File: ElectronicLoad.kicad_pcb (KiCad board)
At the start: 4 copper layers, 100 x 65 mm, 96 parts, among them J1 USB_B, J2 Load, J3 AUX1, J4 TagConnect, J5 ICSP, Q1 MTP3055VL, Q2 DMG2302U, SW2 RESET, SW3 BOOTLOADER, SW4 Control, U1 TLC272, U2 NUP2114, U3 ATmega32U4-AU, U4 MCP1501-20, U5 MCP4726A3T, U6 INA220, U7 PCT2075D, U8 PCT2075D, Y1 16MHz

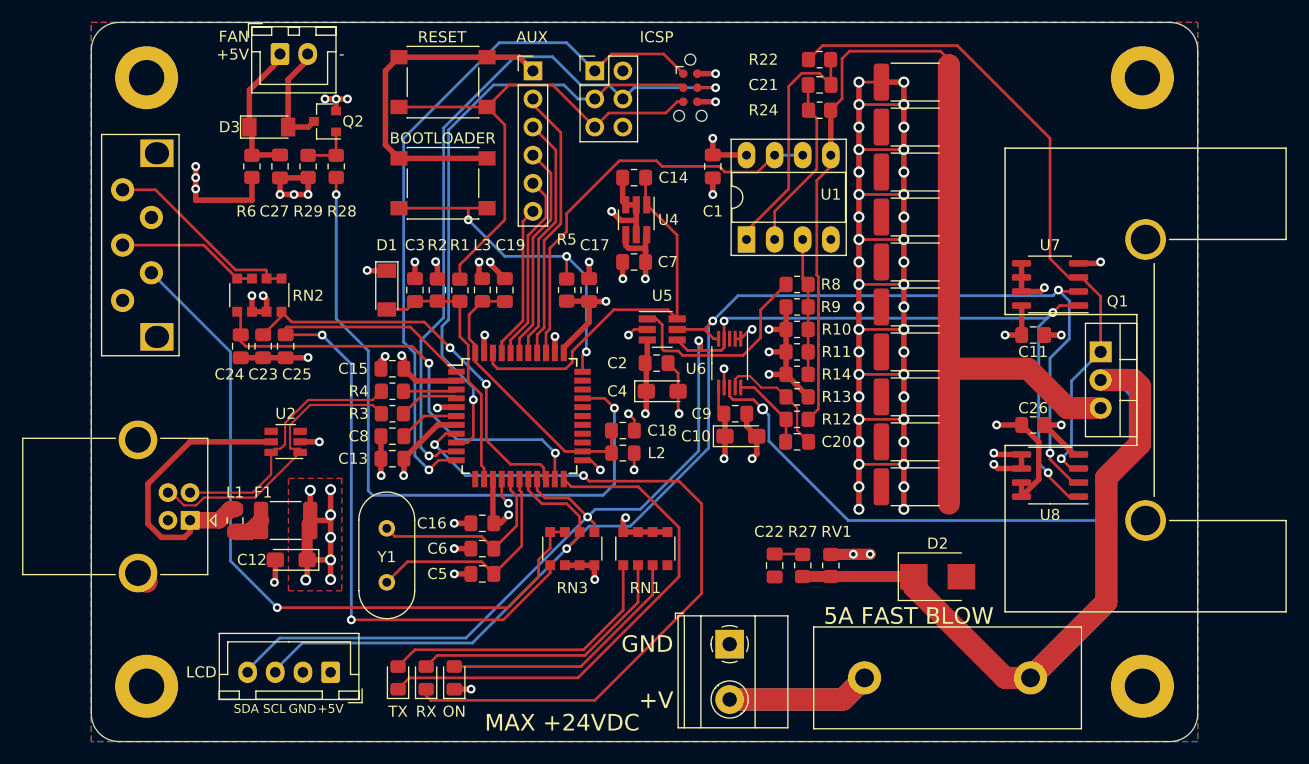
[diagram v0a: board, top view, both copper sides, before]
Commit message: Reduced decoupling capacitance on VBUS to <10uF
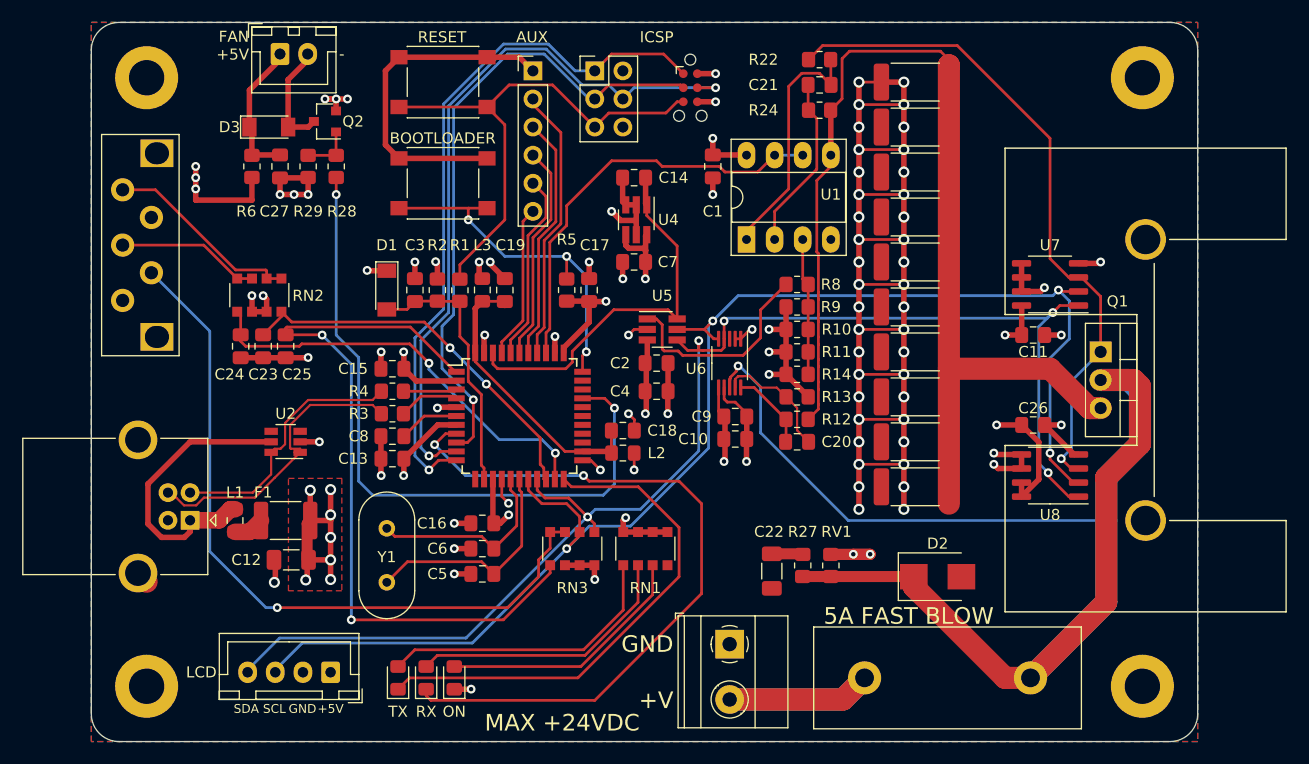
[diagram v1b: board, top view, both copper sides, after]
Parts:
- C10, C4: value 10μF -> 1μF; footprint Capacitor_Tantalum_SMD:CP_EIA-3216-18_Kemet-A_Pad1.58x1.35mm_HandSolder -> Capacitor_SMD:C_0805_2012Metric_Pad1.18x1.45mm_HandSolder
- C12: value 10μF -> 2.2μF; footprint Capacitor_Tantalum_SMD:CP_EIA-3216-18_Kemet-A_Pad1.58x1.35mm_HandSolder -> Capacitor_SMD:C_1206_3216Metric_Pad1.33x1.80mm_HandSolder
- C22: footprint Capacitor_SMD:C_0805_2012Metric_Pad1.18x1.45mm_HandSolder -> Capacitor_SMD:C_1206_3216Metric_Pad1.33x1.80mm_HandSolder
- moved C22 0.57 mm to (111.5, 164.6)
- moved C10 0.57 mm to (108.2, 152.7)
- moved C4 0.51 mm to (101.1, 148.3)
- moved C9 0.25 mm to (108.2, 150.6)
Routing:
- net /SCK: track 54.9 -> 58.2 mm
- net VLOAD: track 134.4 -> 137.3 mm
- net ROT_B: track 40.4 -> 38.3 mm
- net ROT_A: track 36.5 -> 34.9 mm
- net /MOSI: track 64.3 -> 65.8 mm
- net GND: track 301.8 -> 303.1 mm, vias 84 -> 83
- net /MISO: track 65.0 -> 63.8 mm
- net Net-(RN3-Pad3): track 65.6 -> 66.2 mm
- net VCC: track 122.0 -> 122.5 mm

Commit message: Cleanup
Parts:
- removed the C19 at (87.4, 139.2)
- removed J3: AUX1, Connector_PinHeader_2.54mm:PinHeader_1x06_P2.54mm_Vertical
- removed L2: 10μH, Inductor_SMD:L_0805_2012Metric_Pad1.15x1.40mm_HandSolder
- added C18: 100nF, Capacitor_SMD:C_0805_2012Metric_Pad1.18x1.45mm_HandSolder, F.Cu at (97.8, 153.7)
- LCD1: value LCD_2X16-I2C -> OLED 128x64 I2C
- moved C19 16.6 mm to (87.4, 139.2), turned to 90 degrees
- moved R5 15.7 mm to (77.2, 139.2)
- moved C14 9.53 mm to (105.4, 136.1), turned to 90 degrees
- moved U4 4.22 mm to (101.6, 136.3), turned to 180 degrees
- moved C17 3.47 mm to (92.9, 142.0), turned to 180 degrees
- moved J4 3.05 mm to (101.1, 120.9)
- moved J5 3.05 mm to (92.5, 119.4)
- moved D1 1.80 mm to (74.9, 138.9)
- moved C7 1.37 mm to (97.8, 136.1), turned to 90 degrees
- renumbered C18 to C19
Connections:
- U3 pad 24: AVCC -> VCC
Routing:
- net /A1: track 24.9 -> 0.00 mm
- net /A2: track 22.3 -> 0.00 mm
- net /A3: track 19.7 -> 0.00 mm
- net AVCC: track 26.0 -> 7.50 mm
- net /A4: track 17.1 -> 0.00 mm
- net /A5: track 14.0 -> 0.00 mm
- net /~HWB: track 32.6 -> 41.2 mm, vias 3 -> 2
- net VREF2048: track 34.9 -> 28.4 mm
- net /SCK: track 58.2 -> 52.3 mm
- net /MOSI: track 65.8 -> 60.1 mm
- net /MISO: track 63.8 -> 58.7 mm
- net ~EXT_RESET: track 47.0 -> 42.3 mm
- net VLOAD: track 137.3 -> 133.5 mm
- net ILOAD_MCU: track 38.1 -> 35.0 mm
- net GND: track 303.1 -> 300.9 mm, vias 83 -> 82
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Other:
- rule pad_to_mask_clearance: 0.05 -> 0
- board text removed: "A1"
- board text removed: "A2"
- board text removed: "A3"
- board text removed: "A4"
- board text removed: "A5"
- board text removed: "AUX"

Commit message: 3d model for rotary encoder
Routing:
- net VCC: track 124.3 -> 121.5 mm
- net Net-(RN2-Pad1): track 18.1 -> 19.5 mm

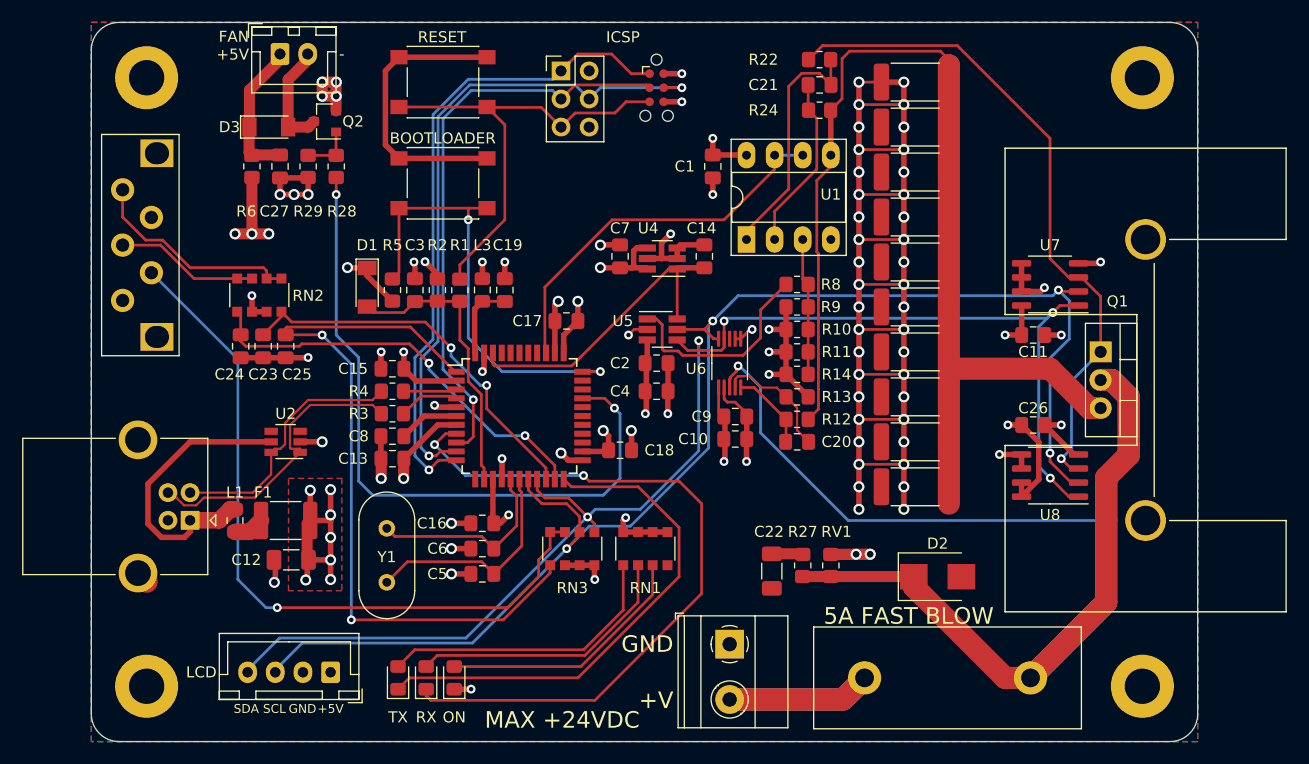
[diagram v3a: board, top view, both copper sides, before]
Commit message: Relabel components
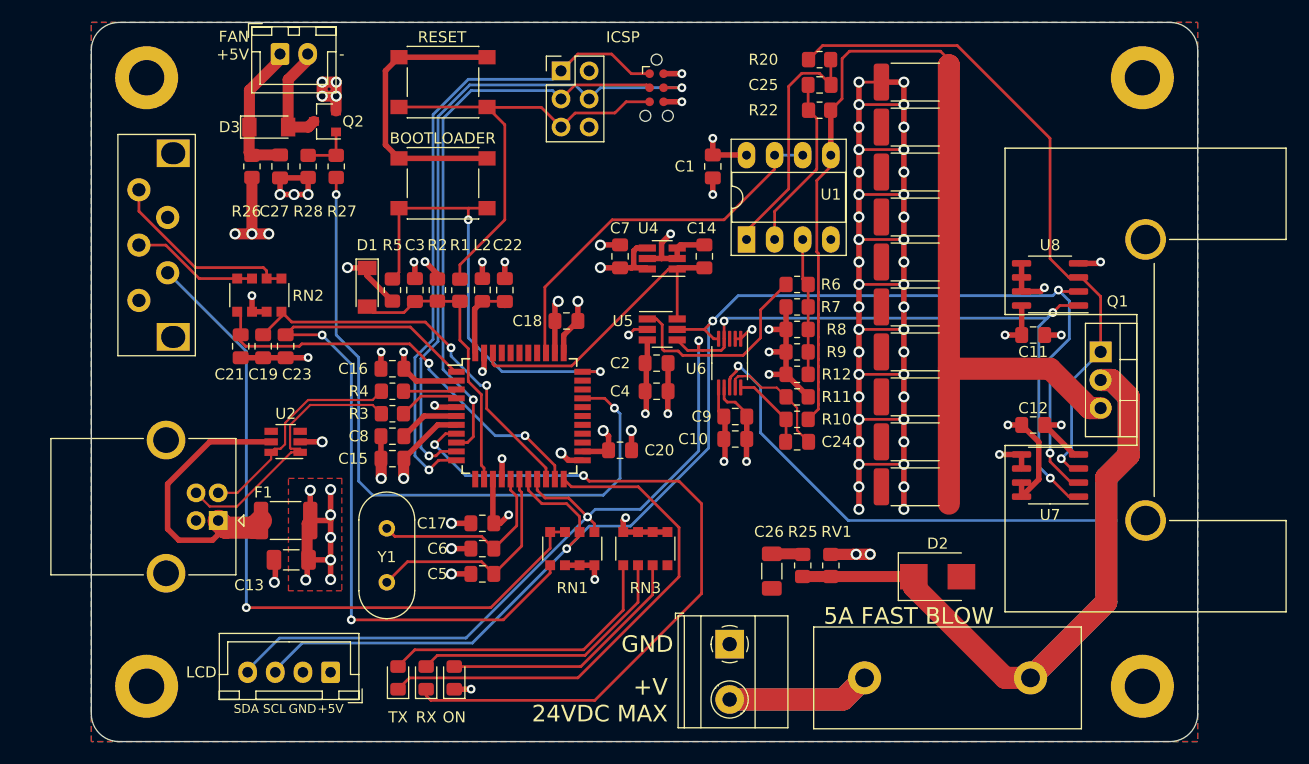
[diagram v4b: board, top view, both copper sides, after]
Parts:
- removed L1: Ferrite, Inductor_SMD:L_0805_2012Metric_Pad1.15x1.40mm_HandSolder
- moved J1 2.54 mm to (61.5, 160.0)
- moved SW3 1.47 mm to (57.4, 135.1)
- renumbered C26 to C12, C12 to C13, C13 to C15, C15 to C16, C16 to C17, C17 to C18, C23 to C19, C18 to C20, C24 to C21, C19 to C22, C25 to C23, C20 to C24, C21 to C25, C22 to C26, J4 to J2, J5 to J3, J2 to J4, L3 to L2, R12 to R10, R13 to R11, R14 to R12, R15 to R13, R16 to R14, R17 to R15, R18 to R16, R19 to R17, R20 to R18, R21 to R19, R22 to R20, R23 to R21, R24 to R22, R25 to R23, R26 to R24, R27 to R25, R6 to R26, R28 to R27, R29 to R28, R8 to R6, R9 to R7, R10 to R8, R11 to R9, RN3 to RN1, RN1 to RN3, SW2 to SW1, SW3 to SW2, SW4 to SW3, U8 to U7, U7 to U8
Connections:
- F1 pad 2: /VUF -> /VBUS
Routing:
- net /D_USB-: track 23.5 -> 20.1 mm
- net /VUF: track 2.77 -> 0.00 mm
- net GND: track 300.9 -> 298.6 mm
- net /D_USB+: track 27.6 -> 25.5 mm
- net Net-(RN2-Pad1): track 19.5 -> 17.7 mm
- net Net-(RN2-Pad3): track 12.9 -> 11.5 mm
- net /VBUS: track 26.4 -> 25.8 mm
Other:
- board text added: "+V 24VDC MAX"
- board text removed: "+V"
- board text removed: "MAX +24VDC"

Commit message: usbC (wip)
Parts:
- added R29: 5K1, Resistor_SMD:R_0805_2012Metric_Pad1.20x1.40mm_HandSolder, F.Cu at (59.3, 149.3)
- added R30: 5K1, Resistor_SMD:R_0805_2012Metric_Pad1.20x1.40mm_HandSolder, F.Cu at (61.4, 149.3)
- J1: value USB_B -> USB_C_Receptacle_USB2.0; footprint DTLib:USB_B_OST_USB-B1HSxx_Horizontal -> DTLib:GCT_USB4105-GF-A
- moved J1 16.2 mm to (51.2, 147.5), turned to 270 degrees
- moved SW3 3.79 mm to (55.0, 132.2)
- moved U2 2.03 mm to (69.6, 152.9), turned to 90 degrees
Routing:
- net /VBUS: track 25.8 -> 0.31 mm
- net /D_USB+: track 25.5 -> 6.76 mm
- net Net-(RN2-Pad1): track 17.7 -> 2.45 mm
- net /D_USB-: track 20.1 -> 6.95 mm
- net VCC: track 121.5 -> 108.6 mm, vias 28 -> 24
- net Net-(RN2-Pad3): track 11.5 -> 1.34 mm
- net Net-(RN1-Pad3): track 65.7 -> 55.7 mm
- net GND: track 298.6 -> 300.9 mm, vias 82 -> 81
- net Net-(J1-PadB5): track 0.00 -> 0.52 mm
